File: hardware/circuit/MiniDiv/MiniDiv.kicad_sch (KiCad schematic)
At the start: 35 parts, among them J1 Conn_01x10_Pin, SW1 SW_DPDT_x2, SW2 SW_DPDT_x2, U1 LM317_TO-263, U2 40106, U3 TL072, U4 40106, U5 CD4040

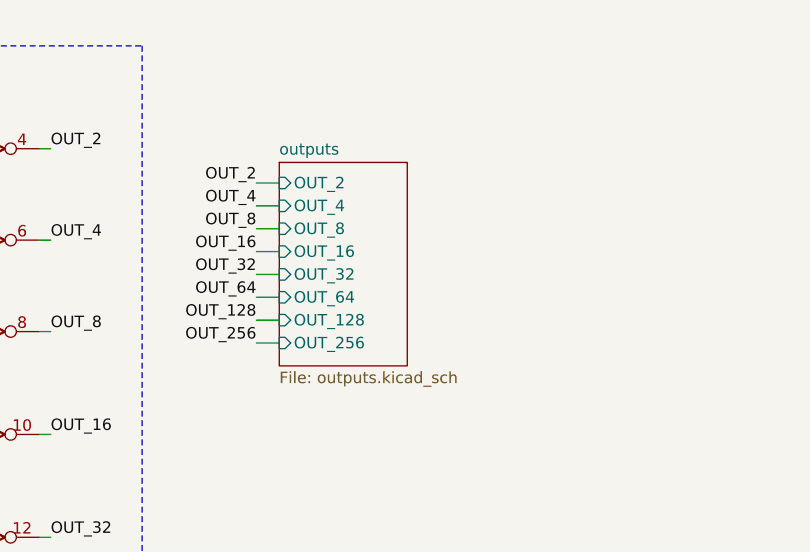
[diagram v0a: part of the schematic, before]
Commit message: reorganized, schem ready for pcb
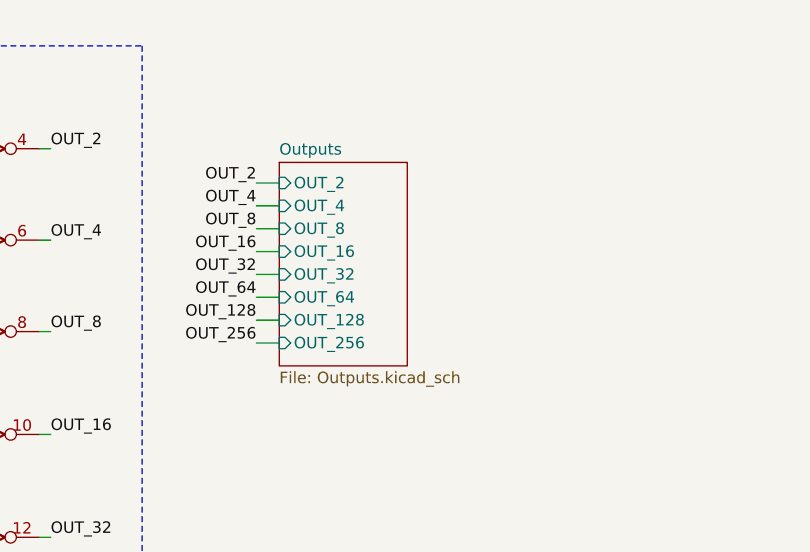
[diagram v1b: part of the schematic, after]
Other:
- sheet outputs renamed Outputs
- sheet Outputs: file outputs.kicad_sch -> Outputs.kicad_sch
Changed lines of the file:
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@@
 			(color 0 0 0 0.0000)
 		)
-		(property "Sheetname" "outputs"
+		(property "Sheetname" "Outputs"
 			(at 208.28 27.4824 0)
 			(effects
@@
 			)
 		)
-		(property "Sheetfile" "outputs.kicad_sch"
+		(property "Sheetfile" "Outputs.kicad_sch"
 			(at 208.28 51.3846 0)
 			(effects
@@
 			)
 		)
+		(property "Field2" ""
+			(at 208.28 28.194 0)
+			(effects
+				(font
+					(size 1.27 1.27)
+				)
+				(hide yes)
+			)
+		)

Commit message: v0.2 PCB
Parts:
- removed C2: 100nF, Capacitor_SMD:C_0603_1608Metric_Pad1.08x0.95mm_HandSolder, symbol Device:C_Small
- removed CLOCK_OUT1: PJ3001F, benjiaomodular:AudioJack_3.5mm, symbol benjiaomodular:PJ3001F
- removed D3: 1N4148, Diode_SMD:D_SOD-123, symbol Diode:1N4148
- removed R1: 10k, Resistor_SMD:R_0603_1608Metric_Pad0.98x0.95mm_HandSolder, symbol Device:R_Small_US
- removed unit 1 of SW1
- removed unit 2 of SW2
- removed U1: LM317_TO-263, Package_TO_SOT_SMD:TO-263-2, symbol Regulator_Linear:LM317_TO-263
- removed U3: TL072, Package_SO:SOIC-8_3.9x4.9mm_P1.27mm, symbol Amplifier_Operational:TL072
- added U2: LM358, Package_SO:SOIC-8_3.9x4.9mm_P1.27mm, symbol Amplifier_Operational:LM358
- added U4: LM317_SOT-223, Package_TO_SOT_SMD:SOT-223-3_TabPin2, symbol Regulator_Linear:LM317_SOT-223
- J1: footprint Connector_IDC:IDC-Header_2x05_P2.54mm_Vertical -> benjiaomodular:Header_IDC2x05_NoArrow
- U5: footprint Package_SO:SOIC-14_3.9x8.7mm_P1.27mm -> Package_SO:SOIC-16_3.9x9.9mm_P1.27mm
- renumbered C3 to C1, C7 to C2, C8 to C3, C1 to C4, C4 to C5, C5 to C6, C6 to C7, D4 to D3, D5 to D4, R2 to R1, R5 to R2, R6 to R3, R9 to R4, R3 to R5, R4 to R6, R10 to R9, SW2 to SW1, U2 to U1, U4 to U3
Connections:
- net +10V: now also U2.8 (V+), U4.2 (VO)
- net +12V: now also R1.1, U4.3 (VI); no longer R1.2
- net CLOCK: now also R4.1, U2.1
- net GND: now also U2.4 (V-); no longer U3.13, U3.9
- net INT_CLOCK: now also CLOCK_IN1.TN
- net RESET: now also U2.7
- net VREF: now also U2.2 (-), U2.6 (-)
- net at SW1.2 (B): now also R1.2; no longer R1.1
- net at R9.2, RV1.3, U1.2: no longer R4.1
- net at D2.1 (K), D3.1 (K), R3.2: now also U2.5 (+)
- net OUT_1024: now reaches U3.12
- net at U5.12 (Q8): now also U3.9
- net at U5.14 (Q9): now also U3.13
- net at D1.1 (K), R2.2: now also U2.3 (+)
- net OUT_512: now reaches U3.8
- net at R5.2, R6.1: now also U4.1 (ADJ)
- no-connect marks 16 -> 8
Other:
- sheet Outputs ports: added OUT_1024, OUT_512; removed none
- moved on the sheet: C7, CLOCK_IN1, D1, D4, R1, R2, R4, R9, RV1, U1A, U3D, U3F

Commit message: Updated PCBs
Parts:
- C1, C4: URL (none) -> https://mou.sr/4ekMsbM
- C2, C3: footprint Capacitor_SMD:CP_Elec_6.3x4.5 -> Capacitor_SMD:CP_Elec_4x3.9; URL (none) -> https://mou.sr/4ekMqRc
- C5, C7: URL (none) -> https://mou.sr/4e5fI6P
- D1, D2, D3: URL (none) -> https://mou.sr/3XEhTbD
- D4: URL (none) -> https://www.taydaelectronics.com/led-3mm-orange.html
- R1, R4: URL (none) -> https://mou.sr/3MINYsI
- R2, R3, R7: URL (none) -> https://mou.sr/4el3qXS
- R9: URL (none) -> https://mou.sr/3MKtPCB
- U1, U3: URL (none) -> https://mou.sr/47m5xIo
- U2: footprint Package_SO:SOIC-8_3.9x4.9mm_P1.27mm -> Package_SO:SOIC-8_5.23x5.23mm_P1.27mm; URL (none) -> https://mou.sr/4dWmV9p
- U5: footprint Package_SO:SOIC-16_3.9x9.9mm_P1.27mm -> Package_SO:SOIC-16W_5.3x10.2mm_P1.27mm

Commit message: updated bom
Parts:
- U5: value CD4040 -> CD4040BNSR; URL (none) -> https://mou.sr/3YF284K
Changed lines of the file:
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@@
 			)
 		)
-		(property "Value" "CD4040"
+		(property "Value" "CD4040BNSR"
 			(at 112.268 45.72 0)
 			(effects
@@
 			)
 		)
-		(property "URL" ""
+		(property "URL" "https://mou.sr/3YF284K"
 			(at 118.11 43.18 0)
 			(effects

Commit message: Added drawings and photos
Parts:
- C1: Manufacturer (none) -> YAGEO; Manufacturers Name YAGEO -> (none); Manufacturers Part Number CC0805KRX7R9BB104 -> (none); Part # (none) -> CC0805KRX7R9BB104
- C2, C3: Manufacturer (none) -> Panasonic; Part # (none) -> EEE-FT1V220AR
- C4: Manufacturer (none) -> YAGEO; Manufacturers Name YAGEO -> (none); Manufacturers Part Number CC0603KRX7R8BB334 -> (none); Part # (none) -> CC0603KRX7R8BB334
- C5, C7: Manufacturer (none) -> Taiyo Yuden; Manufacturers Name Taiyo Yuden -> (none); Manufacturers Part Number TMK212BBJ106KG8T -> (none); Part # (none) -> TMK212BBJ106KG8T
- C6: Manufacturer (none) -> Vishay / Vitramon; Part # (none) -> VJ0805G475KXQTW1BC; URL (none) -> https://mou.sr/4eDk59h
- CLOCK_IN1: Manufacturer (none) -> Tayda Electronics; Part # (none) -> PJ-3001F; URL (none) -> https://www.taydaelectronics.com/pj-3001f-3-5-mm-mono-phone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
- D1, D2, D3: Manufacturer (none) -> Diodes Incorporated; Manufacturers Name Diodes Incorporated -> (none); Manufacturers Part Number 1N4148WQ-7-F -> (none); Part # (none) -> 1N4148WQ-7-F
- D4: Manufacturer (none) -> Tayda Electronics; Manufacturers Name KENTO -> (none); Manufacturers Part Number 3ARG4HWC -> (none); Part # (none) -> LED 3mm Orange
- J1: Manufacturer (none) -> XKB Connectivity; Part # (none) -> X9555WV-2X05-6TV01
- R1: Manufacturer (none) -> YAGEO; Manufacturers Name YAGEO -> (none); Manufacturers Part Number AC0603FR-0710KL -> (none); Part # (none) -> AC0603FR-0710KL
- R2, R3: Manufacturer (none) -> YAGEO; Manufacturers Name YAGEO -> (none); Manufacturers Part Number RC0603FR-07100KL -> (none); Part # (none) -> RC0603FR-07100KL
- R4: Manufacturer (none) -> YAGEO; Part # (none) -> AC0603FR-0710KL
- R5: Manufacturer (none) -> YAGEO; Part # (none) -> RC0603FR-7W470RL; URL (none) -> https://mou.sr/47oY8bq
- R6: Manufacturer (none) -> YAGEO; Part # (none) -> RC0603FR-7W3K3L; URL (none) -> https://mou.sr/4ecU9jY
- R7: Manufacturer (none) -> YAGEO; Part # (none) -> RC0603FR-07100KL
- R8: Manufacturer (none) -> Bourns Inc.; Part # (none) -> CR0603-FX-3302ELF; URL (none) -> https://mou.sr/4ebt4y6
- R9: Manufacturer (none) -> YAGEO; Part # (none) -> RC0603FR-071KL
- RESET_IN1: Manufacturer (none) -> Tayda Electronics; Manufacturers Name Tayda Electronics -> (none); Manufacturers Part Number PJ-3001F -> (none); Part # (none) -> PJ-3001F; URL (none) -> https://www.taydaelectronics.com/pj-3001f-3-5-mm-mono-phone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
- RV1: Manufacturer (none) -> Alpha (Taiwan); Manufacturers Name Alpha (Taiwan) -> (none); Manufacturers Part Number RD901F-40-15R1-B100K -> (none); Part # (none) -> RV09AF-40-20K-B100K; URL (none) -> https://www.taydaelectronics.com/100k-ohm-linear-taper-pote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
- SW1: Manufacturer (none) -> DAIER; Part # (none) -> PB-22E27-ROHS; URL (none) -> https://www.taydaelectronics.com/push-button-switch-dc-30v-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
- U1, U3: Manufacturer (none) -> CD40106BM; Part # (none) -> Texas Instruments
- U2: Manufacturer (none) -> LM358PSR; Part # (none) -> Texas Instruments
- U4: Manufacturer (none) -> LM317DCY; Part # (none) -> Texas Instruments; URL (none) -> https://mou.sr/3UXARYX
- U5: Manufacturer (none) -> CD4040BNSR; Part # (none) -> Texas Instruments

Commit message: Fixed button to momentary
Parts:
- SW1: Manufacturer DAIER -> Tayda Electronics; Part # PB-22E27-ROHS -> KFC7x7 Momentary; URL https://www.taydaelectronics.com/push-button-switch-dc-30v-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 -> https://www.taydaelectronics.com/push-button-switch-momenta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
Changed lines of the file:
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@@
 			)
 		)
-		(property "URL" "https://www.taydaelectronics.com/push-button-switch-dc-30v-0-1a-dpdt-7x7mm.html"
+		(property "URL" "https://www.taydaelectronics.com/push-button-switch-momentary-dc-30v-0-1a-dpdt-7x7mm.html"
 			(at 34.29 83.82 0)
 			(effects
@@
 			)
 		)
-		(property "Manufacturer" "DAIER"
+		(property "Manufacturer" " Tayda Electronics"
 			(at 34.29 83.82 0)
 			(effects
@@
 			)
 		)
-		(property "Part #" "PB-22E27-ROHS"
+		(property "Part #" "KFC7x7 Momentary"
 			(at 34.29 83.82 0)
 			(effects
@@
 			)
 		)
-		(property "URL" "https://www.taydaelectronics.com/push-button-switch-dc-30v-0-1a-dpdt-7x7mm.html"
+		(property "URL" "https://www.taydaelectronics.com/push-button-switch-momentary-dc-30v-0-1a-dpdt-7x7mm.html"
 			(at 256.54 149.86 0)
 			(effects
@@
 			)
 		)
-		(property "Manufacturer" "DAIER"
+		(property "Manufacturer" " Tayda Electronics"
 			(at 256.54 149.86 0)
 			(effects
@@
 			)
 		)
-		(property "Part #" "PB-22E27-ROHS"
+		(property "Part #" "KFC7x7 Momentary"
 			(at 256.54 149.86 0)
 			(effects
